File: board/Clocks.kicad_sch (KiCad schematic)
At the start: 27 parts, among them J17 Front Panel, J4 7.15909MHz, J5 ATX-24, J6 0.89489MHz, J7 1.78977MHz, J8 3.57955MHz, U36 74ACT14, U37 74F191, U38 TL074, U39 YM2151, U40 YM3012, U41 DM1813-10, Y1 14.31818MHz

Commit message: Board V1.1G
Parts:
- U38: footprint Package_DIP:CERDIP-14_W7.62mm_SideBrazed_LongPads_Socket -> Package_DIP:DIP-14_W7.62mm_Socket_LongPads
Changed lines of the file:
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@@
 (kicad_sch
-	(version 20231120)
+	(version 20250114)
 	(generator "eeschema")
-	(generator_version "8.0")
+	(generator_version "9.0")
 	(paper "USLetter")
 	(title_block
 		(title "Sound, Clocks, and Power")
 		(date "2025-03-04")
-		(rev "1.0F")
+		(rev "1.1A")
 		(company "Data Tuning")
 		(comment 1 "Hydra 16")
@@
 	(label "D3"
 		(at 82.55 128.27 0)
-		(fields_autoplaced yes)
 		(effects
 			(font
@@
 	(label "D7"
 		(at 82.55 138.43 0)
-		(fields_autoplaced yes)
 		(effects
 			(font
@@
 	(label "D4"
 		(at 82.55 130.81 0)
-		(fields_autoplaced yes)
 		(effects
 			(font
@@
 	(label "D0"
 		(at 82.55 120.65 0)
-		(fields_autoplaced yes)
 		(effects
 			(font
@@
 	(label "D1"
 		(at 82.55 123.19 0)
-		(fields_autoplaced yes)
 		(effects
 			(font
@@
 	(label "D6"
 		(at 82.55 135.89 0)
-		(fields_autoplaced yes)
 		(effects
 			(font
@@
 	(label "D2"
 		(at 82.55 125.73 0)
-		(fields_autoplaced yes)
 		(effects
 			(font
@@
 	(label "D5"
 		(at 82.55 133.35 0)
-		(fields_autoplaced yes)
 		(effects
 			(font
@@
 			)
 		)
-		(property "Footprint" "Package_DIP:CERDIP-14_W7.62mm_SideBrazed_LongPads_Socket"
+		(property "Footprint" "Package_DIP:DIP-14_W7.62mm_Socket_LongPads"
 			(at 217.17 121.92 0)
 			(effects
@@
 			)
 		)
-		(property "Datasheet" "http://www.ti.com/general/docs/suppproductinfo.tsp?distId=10&gotoUrl=http%3A%2F%2Fwww.ti.com%2Flit%2Fgpn%2Ftl071a"
+		(property "Datasheet" ""
 			(at 217.17 119.38 0)
 			(effects
@@
 			)
 		)
-		(property "Description" "IC OPAMP JFET 4 CIRCUIT 14DIP"
+		(property "Description" ""
 			(at 212.09 127 0)
 			(effects
@@
 			)
 		)
-		(property "Footprint" "Package_DIP:CERDIP-14_W7.62mm_SideBrazed_LongPads_Socket"
+		(property "Footprint" "Package_DIP:DIP-14_W7.62mm_Socket_LongPads"
 			(at 193.04 101.6 0)
 			(effects
@@
 			)
 		)
-		(property "Datasheet" "http://www.ti.com/general/docs/suppproductinfo.tsp?distId=10&gotoUrl=http%3A%2F%2Fwww.ti.com%2Flit%2Fgpn%2Ftl071a"
+		(property "Datasheet" ""
 			(at 193.04 99.06 0)
 			(effects
@@
 			)
 		)
-		(property "Description" "IC OPAMP JFET 4 CIRCUIT 14DIP"
+		(property "Description" ""
 			(at 187.96 106.68 0)
 			(effects
@@
 			)
 		)
-		(property "Footprint" "Package_DIP:CERDIP-14_W7.62mm_SideBrazed_LongPads_Socket"
+		(property "Footprint" "Package_DIP:DIP-14_W7.62mm_Socket_LongPads"
 			(at 217.17 106.68 0)
 			(effects
@@
 			)
 		)
-		(property "Datasheet" "http://www.ti.com/general/docs/suppproductinfo.tsp?distId=10&gotoUrl=http%3A%2F%2Fwww.ti.com%2Flit%2Fgpn%2Ftl071a"
+		(property "Datasheet" ""
 			(at 217.17 104.14 0)
 			(effects
@@
 			)
 		)
-		(property "Description" "IC OPAMP JFET 4 CIRCUIT 14DIP"
+		(property "Description" ""
 			(at 212.09 111.76 0)
 			(effects
@@
 			)
 		)
-		(property "Footprint" "Package_DIP:CERDIP-14_W7.62mm_SideBrazed_LongPads_Socket"
+		(property "Footprint" "Package_DIP:DIP-14_W7.62mm_Socket_LongPads"
 			(at 193.04 133.35 0)
 			(effects
@@
 			)
 		)
-		(property "Datasheet" "http://www.ti.com/general/docs/suppproductinfo.tsp?distId=10&gotoUrl=http%3A%2F%2Fwww.ti.com%2Flit%2Fgpn%2Ftl071a"
+		(property "Datasheet" ""
 			(at 193.04 130.81 0)
 			(effects
@@
 			)
 		)
-		(property "Description" "IC OPAMP JFET 4 CIRCUIT 14DIP"
+		(property "Description" ""
 			(at 187.96 138.43 0)
 			(effects
@@
 		(at 85.09 181.61)
 		(size 21.59 5.08)
+		(exclude_from_sim no)
+		(in_bom yes)
+		(on_board yes)
+		(dnp no)
 		(fields_autoplaced yes)
 		(stroke

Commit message: V1.2B: Final for production.
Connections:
- net GND: no longer C48.1, C49.2, C60.2, C61.2, J5.24 (GND), U40.16 (AGND), U40.8 (AGND)
- new net GNDA: C48.1, C49.2, C60.2, C61.2, J5.24 (GNDA), U40.16 (AGND), U40.8 (AGND)

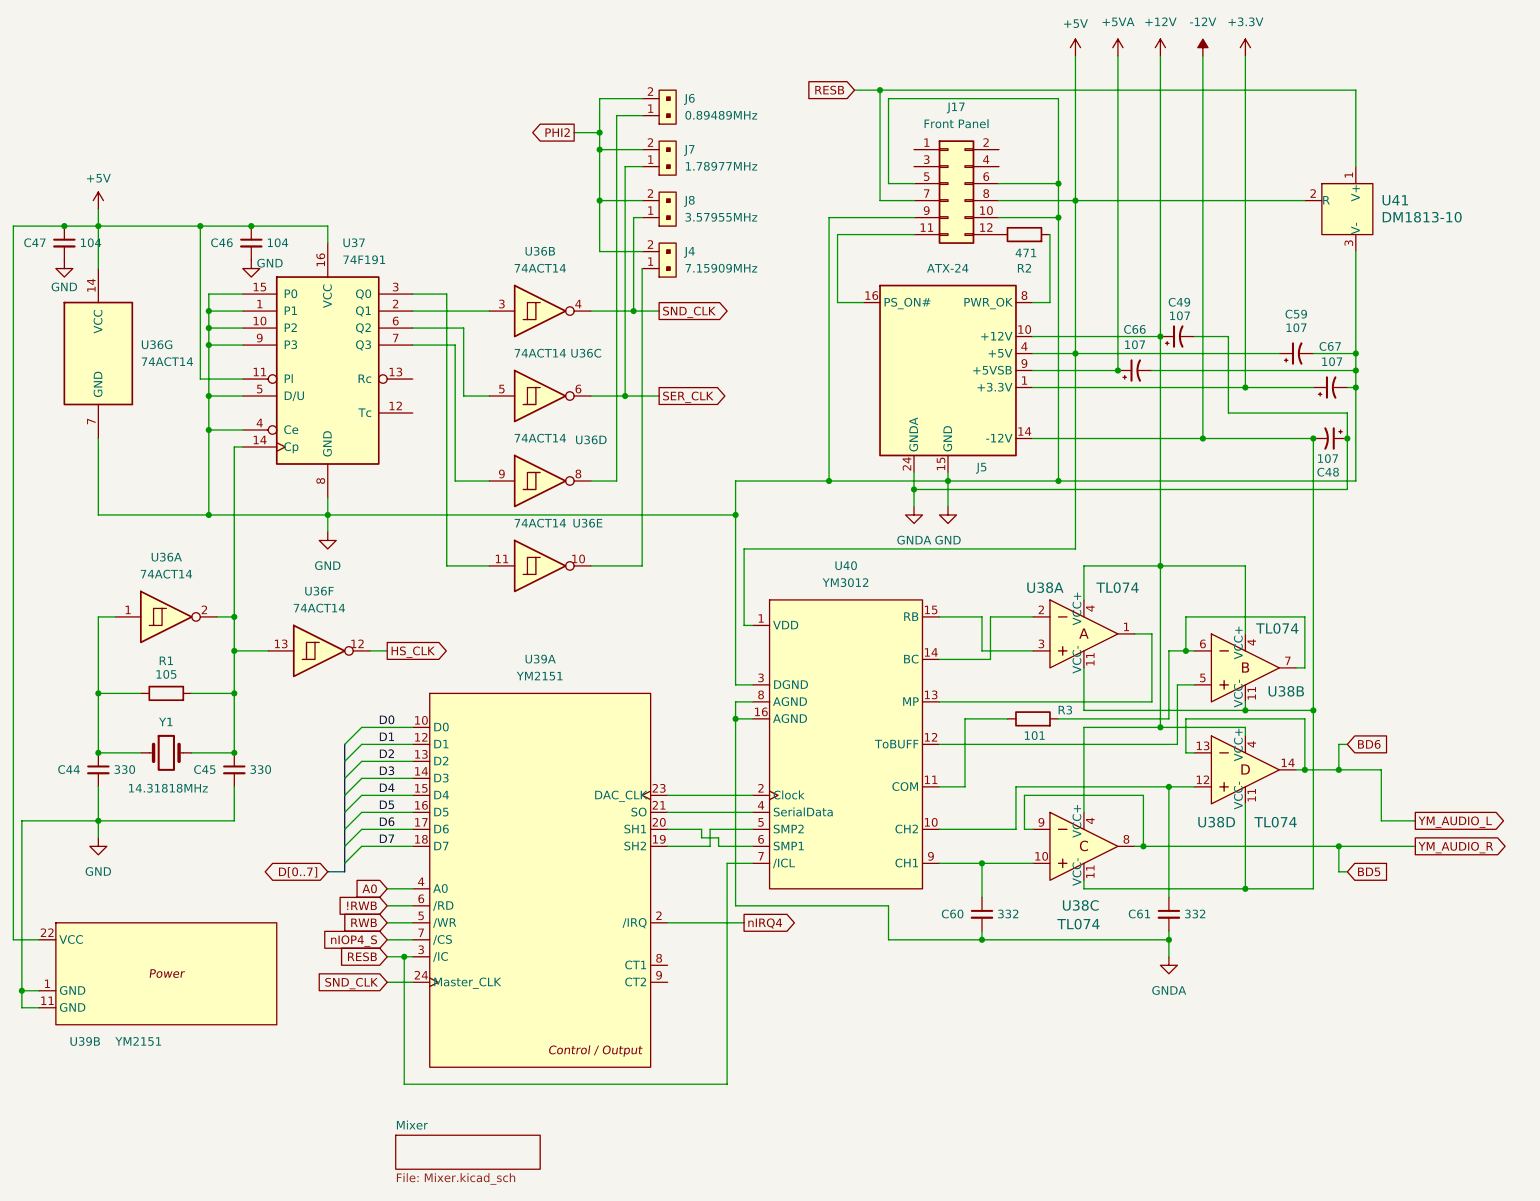
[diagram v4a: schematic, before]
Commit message: Version 1.7A: More rearrangement, partial wiring of PDB, addition of W register
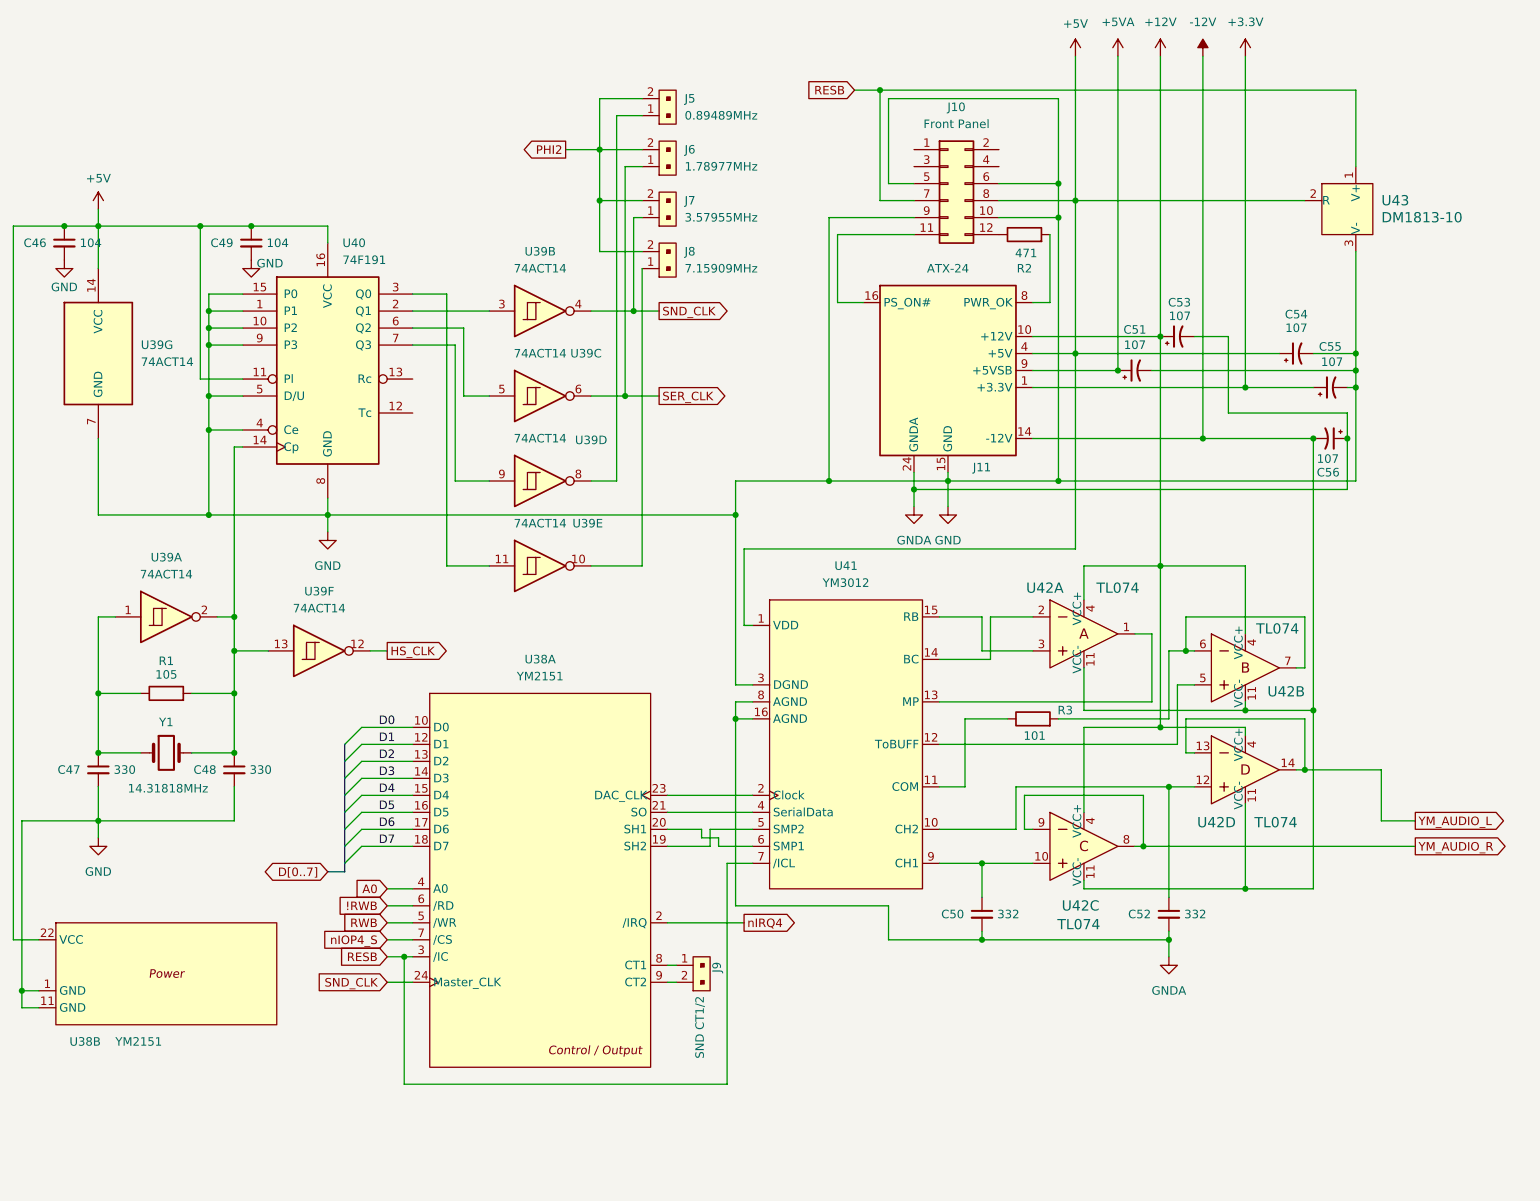
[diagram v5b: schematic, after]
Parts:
- added J9: SND CT1/2, Connector_PinHeader_2.54mm:PinHeader_2x01_P2.54mm_Vertical, symbol dk_Rectangular-Connectors-Headers-Male-Pins:22-23-2021
- renumbered C47 to C46, C44 to C47, C45 to C48, C46 to C49, C60 to C50, C66 to C51, C61 to C52, C49 to C53, C59 to C54, C67 to C55, C48 to C56, J17 to J10, J5 to J11, J6 to J5, J7 to J6, J8 to J7, J4 to J8, U39 to U38, U36 to U39, U37 to U40, U40 to U41, U38 to U42, U41 to U43
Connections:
- net at U38.8 (CT1): now also J9.1
- net at U38.9 (CT2): now also J9.2
- net BD5 renamed YM_AUDIO_R
- net BD6 renamed YM_AUDIO_L
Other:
- removed sheet Mixer

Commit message: V1.8C production board
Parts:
- removed C50, C52: 332, Capacitor_THT:C_Disc_D5.0mm_W2.5mm_P2.50mm, symbol Device:C_Small
- removed J9: SND CT1/2, Connector_PinHeader_2.54mm:PinHeader_2x01_P2.54mm_Vertical, symbol dk_Rectangular-Connectors-Headers-Male-Pins:22-23-2021
- removed R3: 101, Resistor_THT:R_Axial_DIN0204_L3.6mm_D1.6mm_P5.08mm_Horizontal, symbol Device:R
- removed U38: YM2151, Package_DIP:DIP-24_W15.24mm_Socket_LongPads, symbol Yamaha 2151-3012:YM2151
- removed U41: YM3012, Package_DIP:DIP-16_W7.62mm_Socket_LongPads, symbol Yamaha 2151-3012:YM3012
- removed U42: TL074, Package_DIP:DIP-14_W7.62mm_Socket_LongPads, symbol dk_Linear-Amplifiers-Instrumentation-OP-Amps-Buffer-Amps:TL074CN
